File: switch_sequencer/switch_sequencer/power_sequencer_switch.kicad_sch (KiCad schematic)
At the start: 15 parts, among them J13 Eurorack_Power_10pin_Shrouded, U3 AP62200TWU-7, U9 LD1117S50TR_SOT223

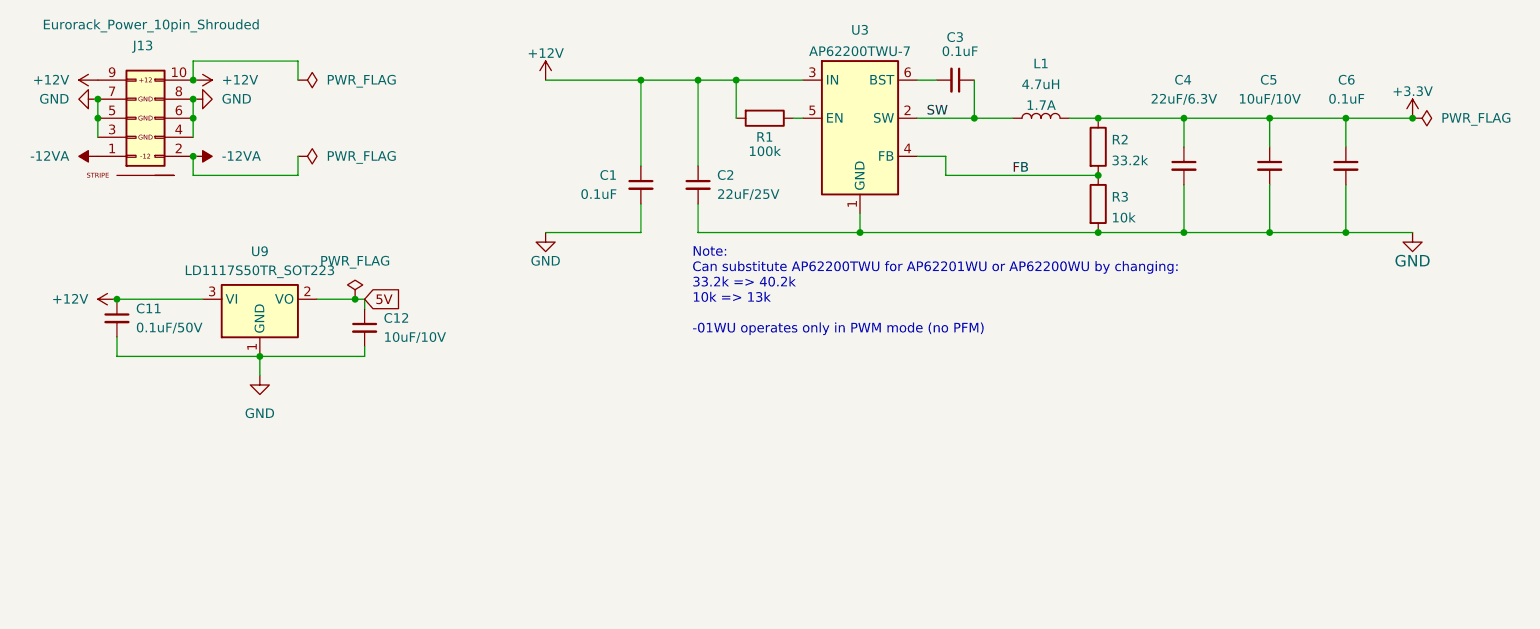
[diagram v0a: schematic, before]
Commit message: Reformated folder structure. Finished layout of sample and hold.
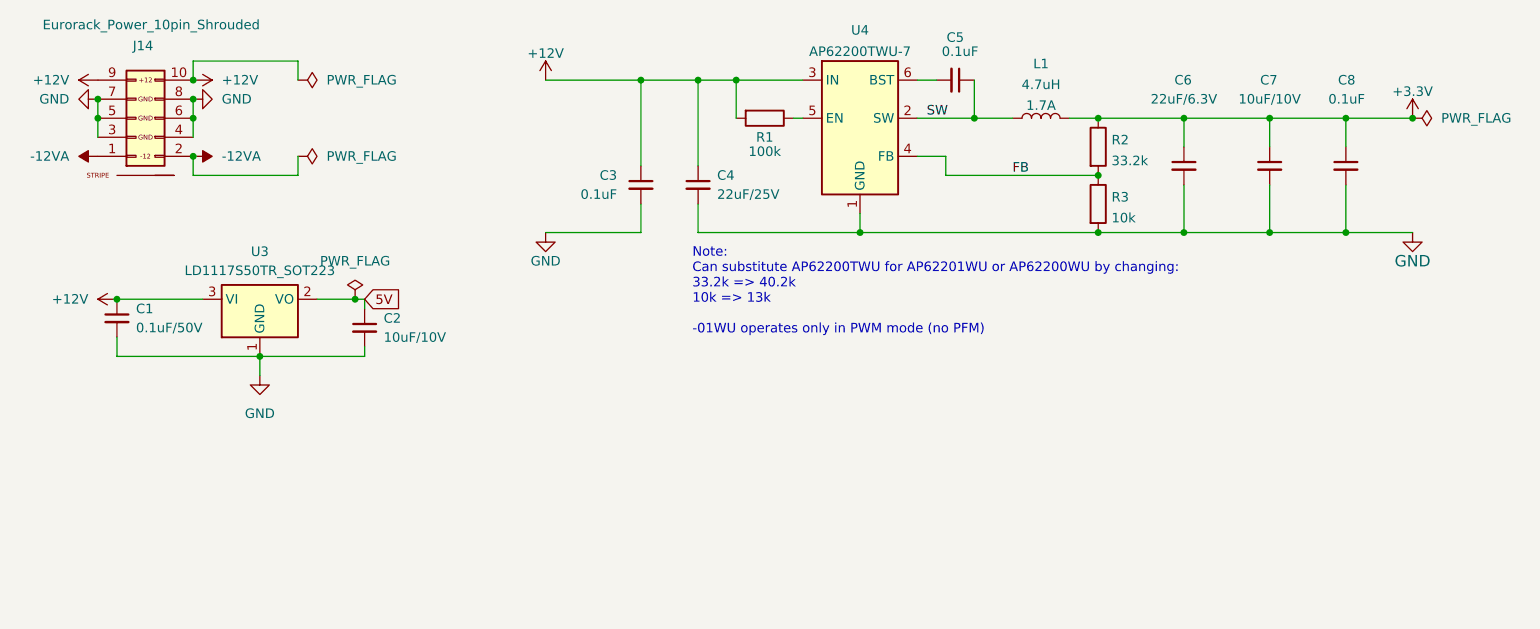
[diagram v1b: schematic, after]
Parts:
- renumbered C11 to C1, C12 to C2, C1 to C3, C2 to C4, C3 to C5, C4 to C6, C5 to C7, C6 to C8, J13 to J14, U9 to U3, U3 to U4

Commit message: sequential switch wip
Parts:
- removed C3, C5, C8: 0.1uF_0603_16V, 4ms_Capacitor:C_0603, symbol 4ms_Capacitor:0.1uF_0603_16V
- removed C4: 22uF_0805_25V, 4ms_Capacitor:C_0805, symbol 4ms_Capacitor:22uF_0805_25V
- removed C6: 22uF_0805_6.3V, 4ms_Capacitor:C_0805, symbol 4ms_Capacitor:22uF_0805_6.3V
- removed C7: 10uF_0603_10V, 4ms_Capacitor:C_0603, symbol 4ms_Capacitor:10uF_0603_10V
- removed L1: 4.7uH_1.2A_40xx, Inductor_SMD:L_Taiyo-Yuden_NR-40xx, symbol 4ms_Inductor:4.7uH_1.2A_40xx
- removed R1: 100k_0603, 4ms_Resistor:R_0603, symbol 4ms_Resistor:100k_0603
- removed R2: 33.2k_0603, 4ms_Resistor:R_0603, symbol 4ms_Resistor:33.2k_0603
- removed R3: 10k_0603, 4ms_Resistor:R_0603, symbol 4ms_Resistor:10k_0603
- removed U4: AP62200TWU-7, 4ms_Package_SOT:TSOT-23-6, symbol 4ms_IC:AP62200TWU-7
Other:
- note removed: "Note: Can substitute AP62200TWU for AP62201WU or AP62200WU by changing: 33.2k => 40.2k 10k => 13k -01WU operates only in PWM mode (no PFM)"

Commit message: sequential swtich more wip
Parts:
- added C10, C11, C12, C13, C14, C3, C4, C5, C6, C7, C8, C9: 0.1uF_0603_16V, 4ms_Capacitor:C_0603, symbol 4ms_Capacitor:0.1uF_0603_16V
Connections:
- net +12V: now also C10.2, C12.2, C14.2, C4.2, C6.2, C8.2
- net -12VA: now also C11.1, C13.1, C3.1, C5.1, C7.1, C9.1
- net GND: no longer J14.4 (GND), J14.6 (GND), J14.8 (GND)
- new net GNDA: C10.1, C11.2, C12.1, C13.2, C14.1, C3.2, C4.1, C5.2, C6.1, C7.2, C8.1, C9.2, J14.4 (GND), J14.6 (GND), J14.8 (GND)

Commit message: sequential switch wip more more
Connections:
- net GNDA is gone; now on net GND: C10.1, C11.2, C12.1, C13.2, C14.1, C3.2, C4.1, C5.2, C6.1, C7.2, C8.1, C9.2, J14.4 (GND), J14.6 (GND), J14.8 (GND)
- net +12V: now also C11.1, C13.1, C3.1, C5.1, C7.1, C9.1; no longer C10.2, C12.2, C14.2, C4.2, C6.2, C8.2
- net -12VA: now also C10.2, C12.2, C14.2, C4.2, C6.2, C8.2; no longer C11.1, C13.1, C3.1, C5.1, C7.1, C9.1
